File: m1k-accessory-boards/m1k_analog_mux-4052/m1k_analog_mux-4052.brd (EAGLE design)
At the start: 20.3 x 50.8 mm, 8 parts, among them IC1 4052N

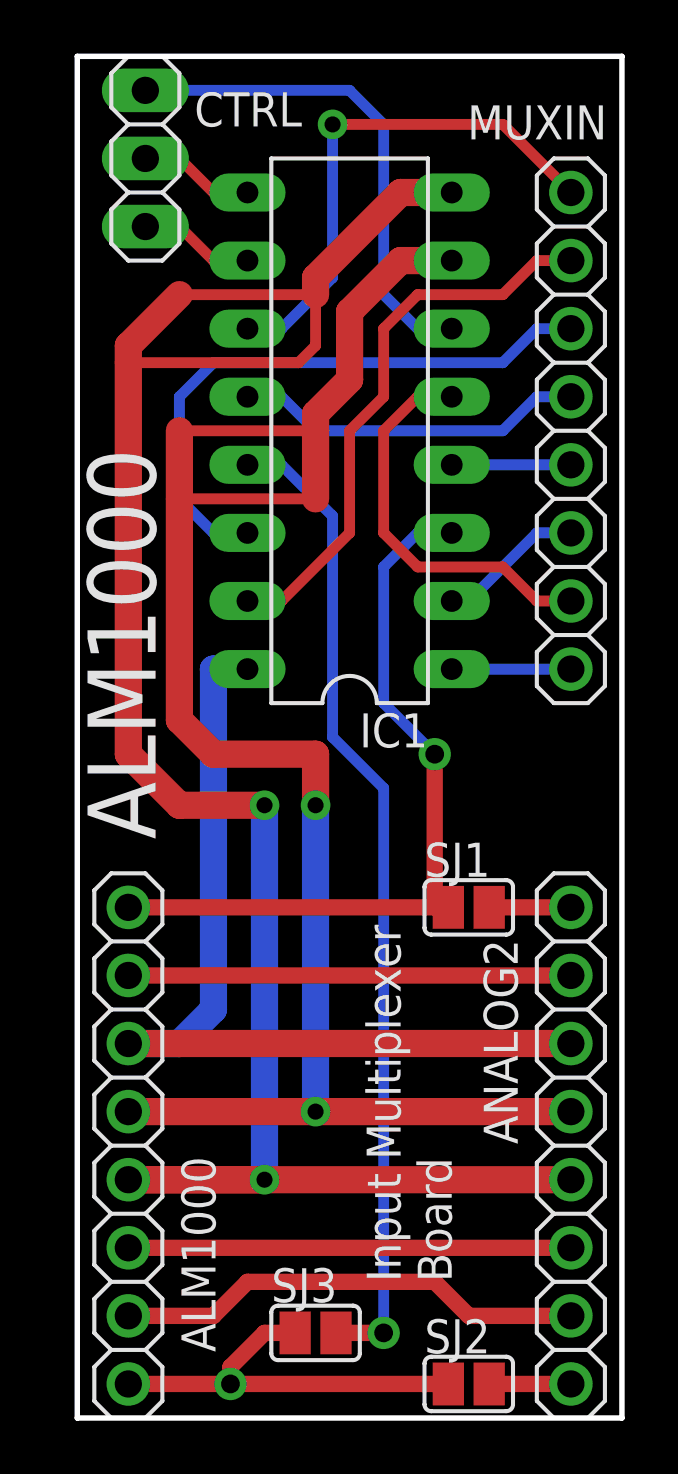
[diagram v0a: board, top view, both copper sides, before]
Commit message: modify header spacing
Moved the analog mux input header on to 0.1" grid centers
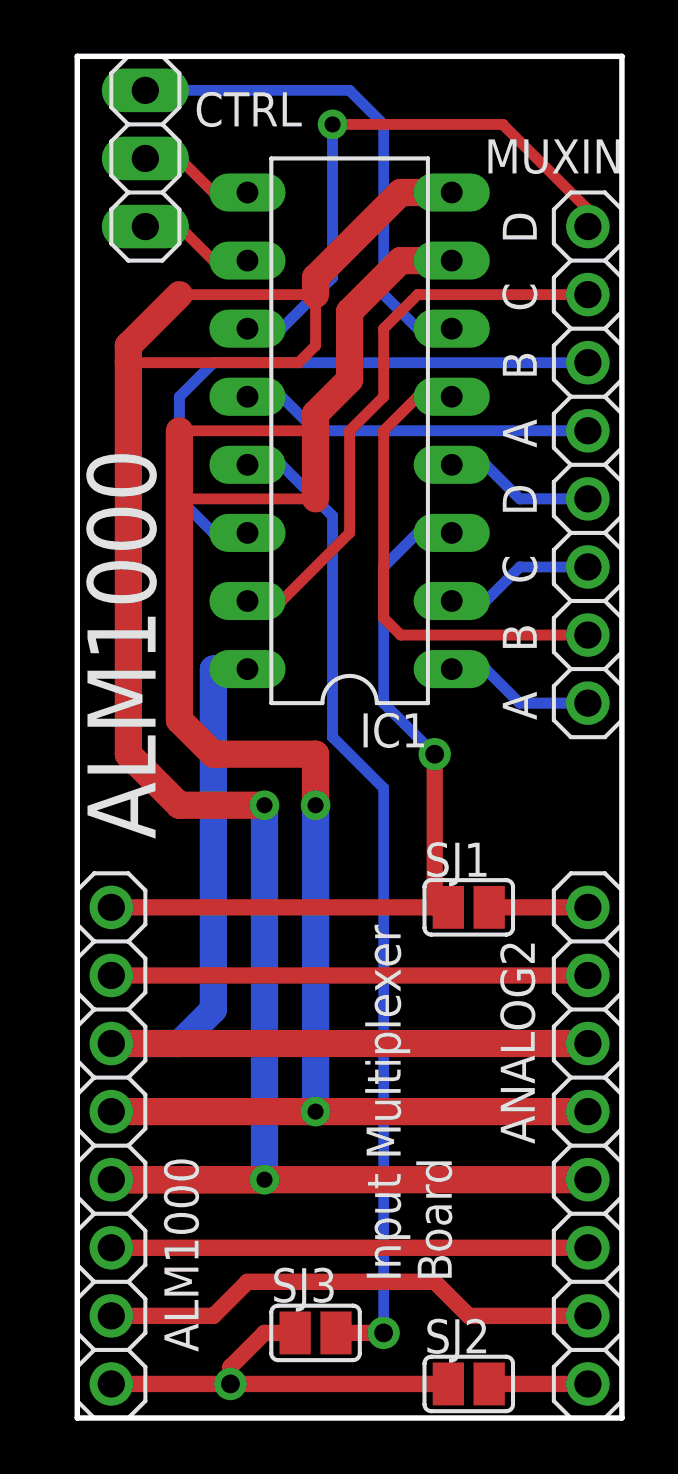
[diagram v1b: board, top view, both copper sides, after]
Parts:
- moved MUXIN 1.42 mm to (19.1, 35.6)
- moved ANALOG2 0.64 mm to (19.1, 10.2)
- moved ALM1000 0.64 mm to (1.27, 10.2)
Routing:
- net N$3: track 14.9 -> 17.9 mm
- net GND: track 80.6 -> 82.5 mm
- net 5V: track 34.2 -> 36.1 mm
- net N$6: track 19.6 -> 21.2 mm
- net CHB: track 16.5 -> 17.8 mm
- net CHA: track 17.6 -> 18.8 mm
- net 2P5V: track 16.5 -> 17.8 mm
- net VEE: track 68.5 -> 69.8 mm
- net N$5: track 4.44 -> 5.61 mm
- net N$1: track 4.44 -> 5.61 mm
- net N$2: track 3.05 -> 3.68 mm
- net N$10: track 3.05 -> 3.68 mm
- net AIN: track 15.5 -> 16.1 mm
- net BIN: track 28.5 -> 29.1 mm
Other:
- board text added: "A"
- board text added: "B"
- board text added: "C"
- board text added: "D"
